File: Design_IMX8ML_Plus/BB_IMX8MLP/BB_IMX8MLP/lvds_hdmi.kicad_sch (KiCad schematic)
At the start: 1 part, among them J7 HDMI_A

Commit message: Add SPB228 WIFI/BLE module
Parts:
- J7: footprint (none) -> Connector_Video:HDMI_A_Molex_208658-1001_Horizontal
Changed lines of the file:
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@@
-(kicad_sch (version 20230121) (generator eeschema)
-  (paper "A4")
-  (symbol (lib_id "Connector:HDMI_A") (at 242.57 74.93 0) (unit 1)
-    (in_bom yes) (on_board yes) (dnp no) (fields_autoplaced)
-    (property "Reference" "J7" (at 254 73.66 0)
-      (effects (font (size 1.27 1.27)) (justify left))
-    )
-    (property "Value" "HDMI_A" (at 254 76.2 0)
-      (effects (font (size 1.27 1.27)) (justify left))
-    )
-    (property "Footprint" "" (at 243.205 74.93 0)
-      (effects (font (size 1.27 1.27)) hide)
-    )
-    (property "Datasheet" "https://en.wikipedia.org/wiki/HDMI" (at 243.205 74.93 0)
-      (effects (font (size 1.27 1.27)) hide)
-    )
-    (pin "1")
-    (pin "10")
-    (pin "11")
-    (pin "12")
-    (pin "13")
-    (pin "14")
-    (pin "15")
-    (pin "16")
-    (pin "17")
-    (pin "18")
-    (pin "19")
-    (pin "2")
-    (pin "3")
-    (pin "4")
-    (pin "5")
-    (pin "6")
-    (pin "7")
-    (pin "8")
-    (pin "9")
-    (pin "SH")
-    (instances
-      (project "BB_IMX8MLP"
-        (path "/cd2fb234-91e5-476f-84ed-38419b628dc6/fabf144f-7078-4de8-86ad-539ef5f82b16"
-          (reference "J7") (unit 1)
-        )
-      )
-    )
-  )
+(kicad_sch
+	(version 20231120)
+	(generator "eeschema")
+	(generator_version "8.0")
+	(paper "A4")
+	(symbol
+		(lib_id "Connector:HDMI_A")
+		(at 242.57 74.93 0)
+		(unit 1)
+		(exclude_from_sim no)
+		(in_bom yes)
+		(on_board yes)
+		(dnp no)
+		(fields_autoplaced yes)
+		(property "Reference" "J7"
+			(at 254 73.66 0)
+			(effects
+				(font
+					(size 1.27 1.27)
+				)
+				(justify left)
+			)
+		)
+		(property "Value" "HDMI_A"
+			(at 254 76.2 0)
+			(effects
+				(font
+					(size 1.27 1.27)
+				)
+				(justify left)
+			)
+		)
+		(property "Footprint" "Connector_Video:HDMI_A_Molex_208658-1001_Horizontal"
+			(at 243.205 74.93 0)
+			(effects
+				(font
+					(size 1.27 1.27)
+				)
+				(hide yes)
+			)
+		)
+		(property "Datasheet" "https://en.wikipedia.org/wiki/HDMI"
+			(at 243.205 74.93 0)
+			(effects
+				(font
+					(size 1.27 1.27)
+				)
+				(hide yes)
+			)
+		)
+		(property "Description" ""
+			(at 242.57 74.93 0)
+			(effects
+				(font
+					(size 1.27 1.27)
+				)
+				(hide yes)
+			)
+		)
+		(pin "1"
+		)
+		(pin "10"
+		)
+		(pin "11"
+		)
+		(pin "12"
+		)
+		(pin "13"
+		)
+		(pin "14"
+		)
+		(pin "15"
+		)
+		(pin "16"
+		)
+		(pin "17"
+		)
+		(pin "18"
+		)
+		(pin "19"
+		)
+		(pin "2"
+		)
+		(pin "3"
+		)
+		(pin "4"
+		)
+		(pin "5"
+		)
+		(pin "6"
+		)
+		(pin "7"
+		)
+		(pin "8"
+		)
+		(pin "9"
+		)
+		(pin "SH"
+		)
+		(instances
+			(project "BB_IMX8MLP"
+				(path "/cd2fb234-91e5-476f-84ed-38419b628dc6/fabf144f-7078-4de8-86ad-539ef5f82b16"
+					(reference "J7")
+					(unit 1)
+				)
+			)
+		)
+	)
 )

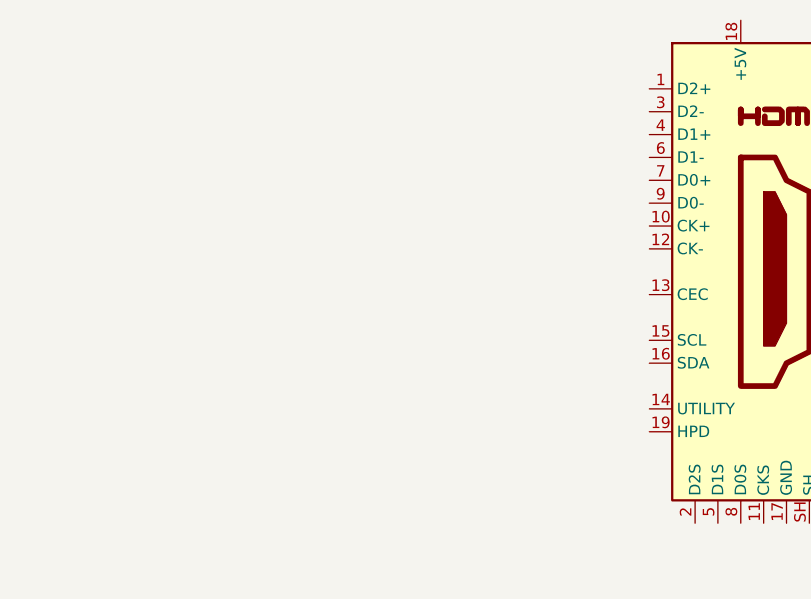
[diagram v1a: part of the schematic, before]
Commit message: Improve power source module in the base board
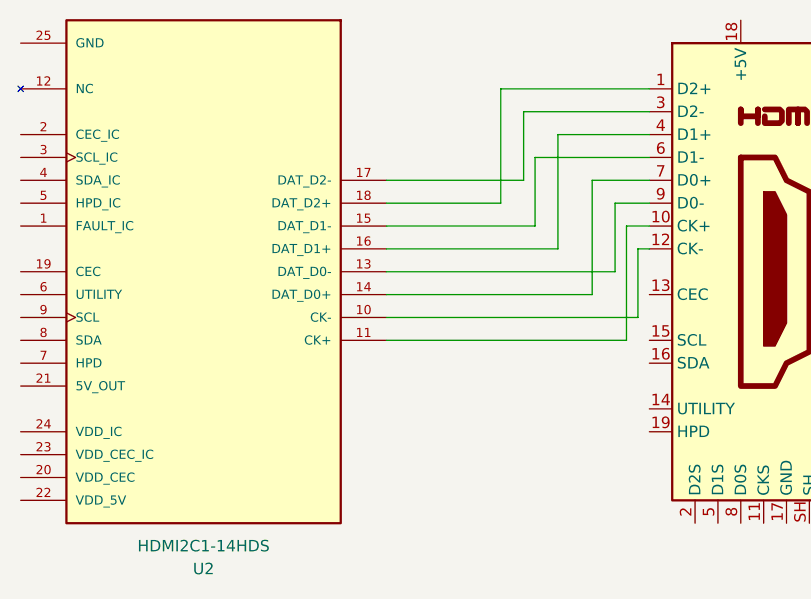
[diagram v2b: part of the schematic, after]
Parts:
- added U2: HDMI2C1-14HDS, Package_DFN_QFN:VQFN-24-1EP_4x4mm_P0.5mm_EP2.5x2.5mm, symbol HDMI2C1-14HDS:HDMI2C1-14HDS
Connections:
- net at J7.1 (D2+): now also U2.18 (DAT_D2+)
- net at J7.10 (CK+): now also U2.11 (CK+)
- net at J7.12 (CK-): now also U2.10 (CK-)
- net at J7.3 (D2-): now also U2.17 (DAT_D2-)
- net at J7.4 (D1+): now also U2.16 (DAT_D1+)
- net at J7.6 (D1-): now also U2.15 (DAT_D1-)
- net at J7.7 (D0+): now also U2.14 (DAT_D0+)
- net at J7.9 (D0-): now also U2.13 (DAT_D0-)

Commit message: improving the usb conector
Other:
- moved on the sheet: J7

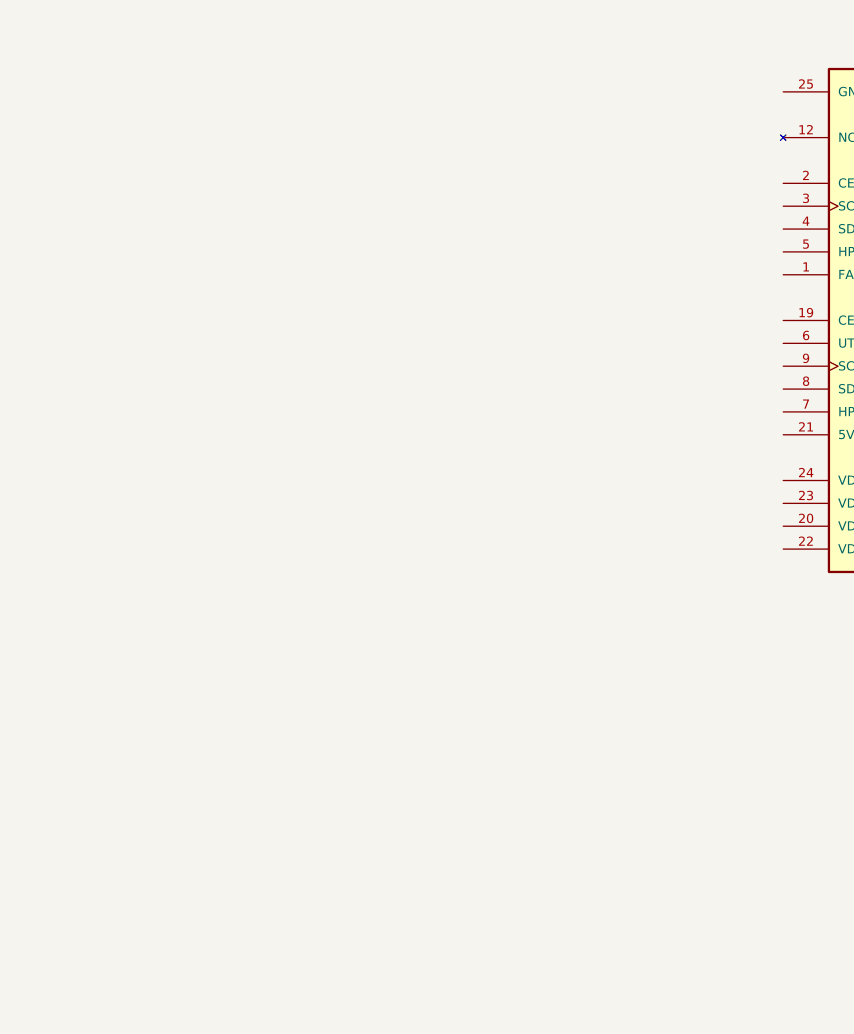
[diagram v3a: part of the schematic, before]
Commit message: improving Ethernet, USB and Camera inteface
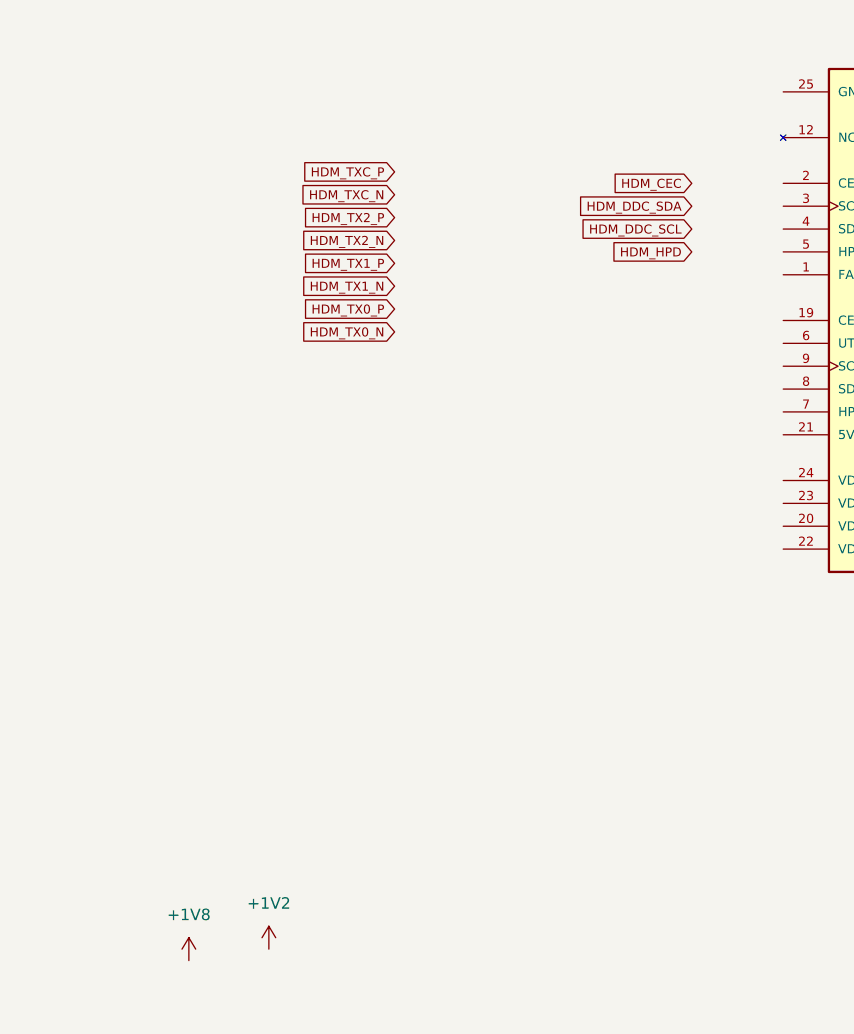
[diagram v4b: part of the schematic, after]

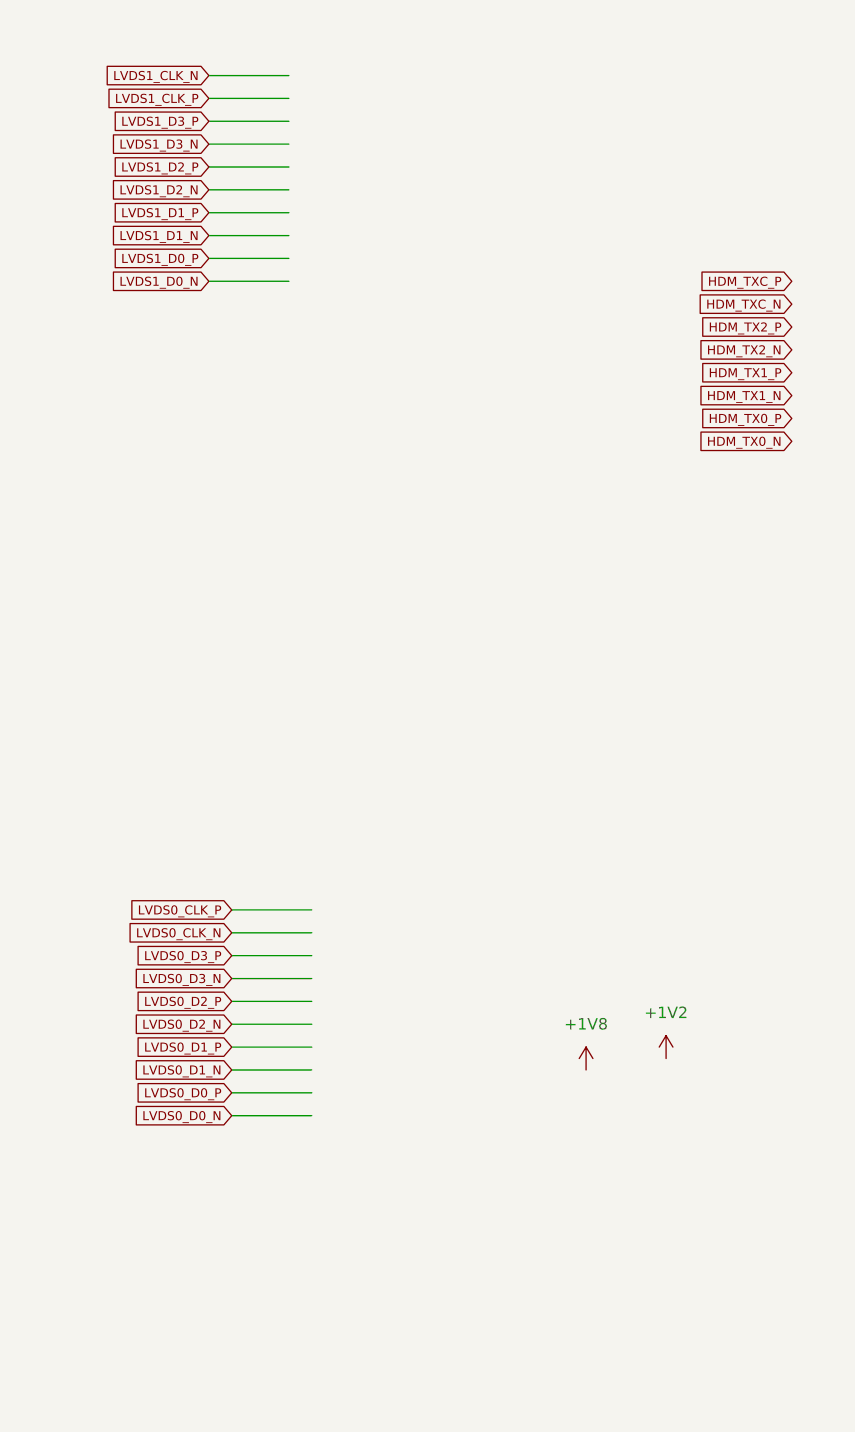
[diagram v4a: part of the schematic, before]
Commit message: Add LVDs and CSI Interface
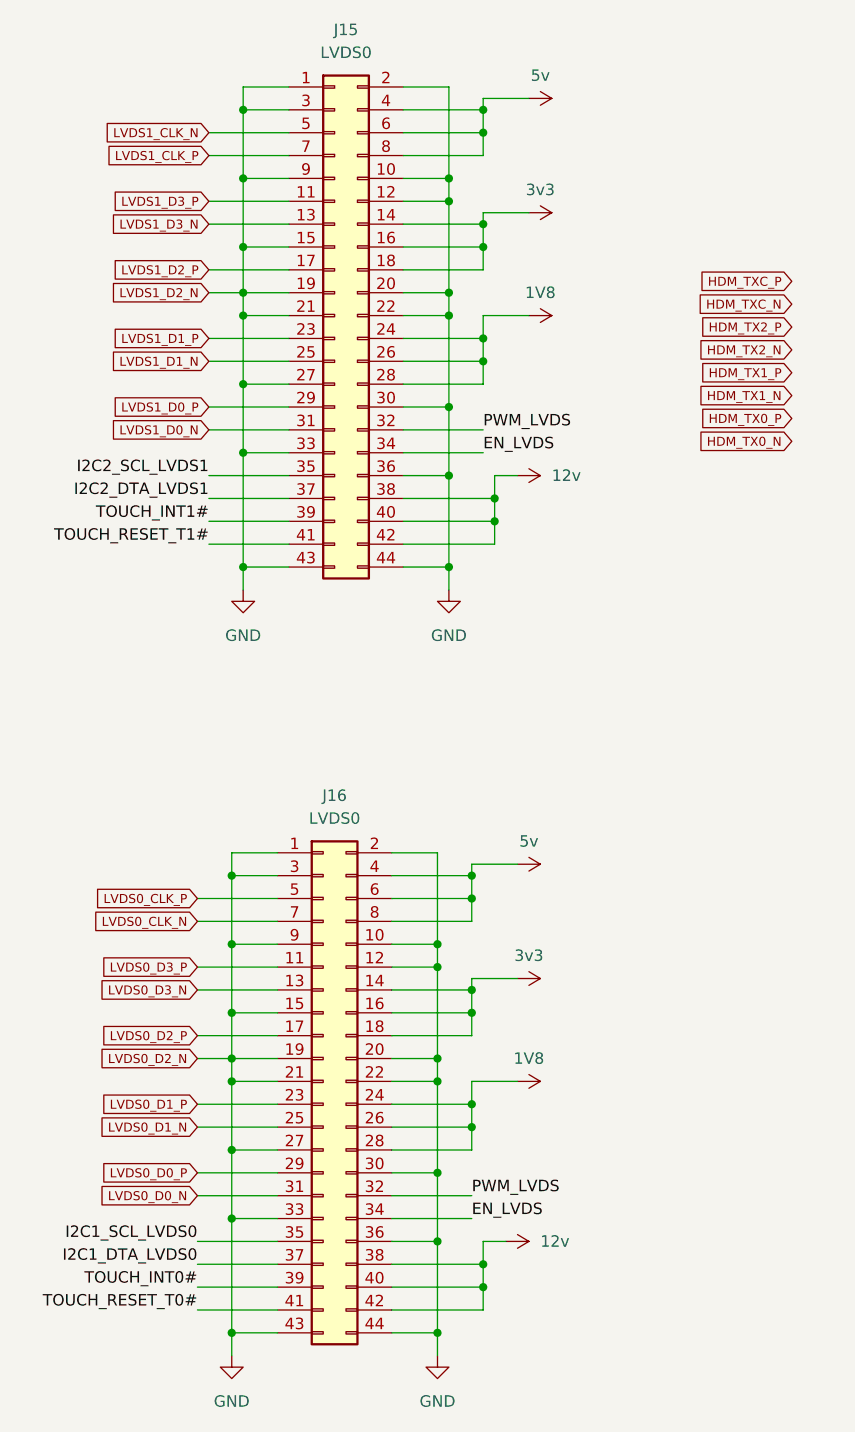
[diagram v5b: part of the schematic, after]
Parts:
- added J15, J16: LVDS0, symbol Connector_Generic:Conn_02x22_Odd_Even
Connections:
- net LVDS0_CLK_N: now also J16.7 (Pin_7)
- net LVDS0_CLK_P: now also J16.5 (Pin_5)
- net LVDS0_D0_N: now also J16.31 (Pin_31)
- net LVDS0_D0_P: now also J16.29 (Pin_29)
- net LVDS0_D1_N: now also J16.25 (Pin_25)
- net LVDS0_D1_P: now also J16.23 (Pin_23)
- net LVDS0_D2_P: now also J16.17 (Pin_17)
- net LVDS0_D3_N: now also J16.13 (Pin_13)
- net LVDS0_D3_P: now also J16.11 (Pin_11)
- net LVDS1_CLK_N: now also J15.5 (Pin_5)
- net LVDS1_CLK_P: now also J15.7 (Pin_7)
- net LVDS1_D0_N: now also J15.31 (Pin_31)
- net LVDS1_D0_P: now also J15.29 (Pin_29)
- net LVDS1_D1_N: now also J15.25 (Pin_25)
- net LVDS1_D1_P: now also J15.23 (Pin_23)
- net LVDS1_D2_P: now also J15.17 (Pin_17)
- net LVDS1_D3_N: now also J15.13 (Pin_13)
- net LVDS1_D3_P: now also J15.11 (Pin_11)
- new net 12v: J15.38 (Pin_38), J15.40 (Pin_40), J15.42 (Pin_42), J16.38 (Pin_38), J16.40 (Pin_40), J16.42 (Pin_42)
- new net 1V8: J15.24 (Pin_24), J15.26 (Pin_26), J15.28 (Pin_28), J16.24 (Pin_24), J16.26 (Pin_26), J16.28 (Pin_28)
- new net 3v3: J15.14 (Pin_14), J15.16 (Pin_16), J15.18 (Pin_18), J16.14 (Pin_14), J16.16 (Pin_16), J16.18 (Pin_18)
- new net 5v: J15.4 (Pin_4), J15.6 (Pin_6), J15.8 (Pin_8), J16.4 (Pin_4), J16.6 (Pin_6), J16.8 (Pin_8)
- new net EN_LVDS: J15.34 (Pin_34), J16.34 (Pin_34)
- new net GND: J15.1 (Pin_1), J15.10 (Pin_10), J15.12 (Pin_12), J15.15 (Pin_15), J15.19 (Pin_19), J15.2 (Pin_2), J15.20 (Pin_20), J15.21 (Pin_21), J15.22 (Pin_22), J15.27 (Pin_27), J15.3 (Pin_3), J15.30 (Pin_30), J15.33 (Pin_33), J15.36 (Pin_36), J15.43 (Pin_43), J15.44 (Pin_44), J15.9 (Pin_9), J16.1 (Pin_1), J16.10 (Pin_10), J16.12 (Pin_12), J16.15 (Pin_15), J16.19 (Pin_19), J16.2 (Pin_2), J16.20 (Pin_20), J16.21 (Pin_21), J16.22 (Pin_22), J16.27 (Pin_27), J16.3 (Pin_3), J16.30 (Pin_30), J16.33 (Pin_33), J16.36 (Pin_36), J16.43 (Pin_43), J16.44 (Pin_44), J16.9 (Pin_9)
- new net I2C1_DTA_LVDS0: J16.37 (Pin_37)
- new net I2C1_SCL_LVDS0: J16.35 (Pin_35)
- new net I2C2_DTA_LVDS1: J15.37 (Pin_37)
- new net I2C2_SCL_LVDS1: J15.35 (Pin_35)
- new net PWM_LVDS: J15.32 (Pin_32), J16.32 (Pin_32)
- new net TOUCH_INT0#: J16.39 (Pin_39)
- new net TOUCH_INT1#: J15.39 (Pin_39)
- new net TOUCH_RESET_T0#: J16.41 (Pin_41)
- new net TOUCH_RESET_T1#: J15.41 (Pin_41)
